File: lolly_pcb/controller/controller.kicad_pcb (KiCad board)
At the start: 2 copper layers, 93.8 x 60.6 mm, 81 parts, among them J1 Conn_01x02_Pin, SW1 SW_SPDT, U1 ESP32-S2-MINI-1

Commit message: use pin no. 5 for button
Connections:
- U1 pad VBUS: VBUS -> (no net)
- U4 pad 1: 11 -> 5
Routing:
- net VBUS: track 87.8 -> 11.1 mm, vias 2 -> 0
- net 11: track 96.3 -> 70.1 mm, vias 4 -> 3
- net 5: track 71.2 -> 93.4 mm, vias 3 -> 5
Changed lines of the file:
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@@
 			(layers "*.Cu" "*.Mask")
 			(remove_unused_layers no)
-			(net 9 "11")
+			(net 25 "5")
 			(pinfunction "In1")
 			(pintype "input")
@@
 			(layers "*.Cu" "*.Mask")
 			(remove_unused_layers no)
-			(net 30 "VBUS")
 		)
 	)
@@
 	)
 	(gr_text "Bat+\n"
-		(at 155.461 135.56 0)
+		(at 145.682 132.385 0)
 		(layer "B.SilkS")
 		(effects
@@
 	)
 	(gr_text "Bat -\n"
-		(at 161.938 127.813 0)
+		(at 153.048 132.385 0)
 		(layer "B.SilkS")
 		(effects
@@
 	)
 	(segment
-		(start 147.46 140.64)
-		(end 153.81 134.29)
-		(width 0.2)
-		(layer "F.Cu")
-		(net 9)
-	)
-	(segment
 		(start 117.742 123.114)
 		(end 116.98 122.352)
@@
 	)
 	(segment
-		(start 147.46 148.514)
-		(end 147.46 140.64)
-		(width 0.2)
-		(layer "F.Cu")
-		(net 9)
-	)
-	(segment
 		(start 145.682 122.86)
 		(end 145.428 123.114)
@@
 	)
 	(via
-		(at 153.81 134.29)
-		(size 0.6)
-		(drill 0.3)
-		(layers "F.Cu" "B.Cu")
-		(net 9)
-	)
-	(via
 		(at 145.682 122.86)
 		(size 0.6)
@@
 	)
 	(segment
-		(start 153.81 134.29)
-		(end 153.81 126.67)
-		(width 0.2)
-		(layer "B.Cu")
-		(net 9)
-	)
-	(segment
-		(start 156.604 125.4)
-		(end 155.08 125.4)
+		(start 148.222 125.4)
+		(end 156.604 125.4)
 		(width 0.2)
 		(layer "B.Cu")
@@
 	)
 	(segment
-		(start 153.81 126.67)
-		(end 155.08 125.4)
-		(width 0.2)
-		(layer "B.Cu")
-		(net 9)
-	)
-	(segment
-		(start 155.08 125.4)
-		(end 148.222 125.4)
-		(width 0.2)
-		(layer "B.Cu")
-		(net 9)
-	)
-	(segment
 		(start 148.222 125.4)
 		(end 145.682 122.86)
@@
 	)
 	(segment
+		(start 147.46 135.687)
+		(end 149.365 133.782)
+		(width 0.2)
+		(layer "F.Cu")
+		(net 25)
+	)
+	(segment
 		(start 124.6 120.066)
 		(end 124.6 107.62)
@@
 	)
 	(segment
+		(start 147.46 148.514)
+		(end 147.46 135.687)
+		(width 0.2)
+		(layer "F.Cu")
+		(net 25)
+	)
+	(segment
 		(start 146.698 127.686)
 		(end 143.396 124.384)
@@
 	)
 	(via
+		(at 150.762 127.686)
+		(size 0.6)
+		(drill 0.3)
+		(layers "F.Cu" "B.Cu")
+		(net 25)
+	)
+	(via
 		(at 161.176 127.686)
 		(size 0.6)
@@
 		(net 25)
 	)
+	(via
+		(at 149.365 133.782)
+		(size 0.6)
+		(drill 0.3)
+		(layers "F.Cu" "B.Cu")
+		(net 25)
+	)
 	(segment
 		(start 174.384 127.686)
@@
 	)
 	(segment
+		(start 150 128.448)
+		(end 150.762 127.686)
+		(width 0.2)
+		(layer "B.Cu")
+		(net 25)
+	)
+	(segment
 		(start 131.204 122.352)
 		(end 131.712 122.86)
@@
 	)
 	(segment
+		(start 149.365 133.782)
+		(end 150 133.147)
+		(width 0.2)
+		(layer "B.Cu")
+		(net 25)
+	)
+	(segment
+		(start 150 133.147)
+		(end 150 128.448)
+		(width 0.2)
+		(layer "B.Cu")
+		(net 25)
+	)
+	(segment
 		(start 143.269 124.384)
 		(end 143.396 124.384)
@@
 	)
 	(segment
-		(start 158.5 111.5)
-		(end 158.5 109.1)
-		(width 0.5)
-		(layer "F.Cu")
-		(net 30)
-	)
-	(via
-		(at 158.5 111.5)
-		(size 0.6)
-		(drill 0.3)
-		(layers "F.Cu" "B.Cu")
-		(net 30)
-	)
-	(via
-		(at 158.5 109.1)
-		(size 0.6)
-		(drill 0.3)
-		(layers "F.Cu" "B.Cu")
-		(net 30)
-	)
-	(segment
-		(start 161.6 140.6)
-		(end 161.6 139.032)
-		(width 0.5)
-		(layer "B.Cu")
-		(net 30)
-	)
-	(segment
 		(start 168.844179 146.986364)
 		(end 165.486364 146.986364)
@@
 	)
 	(segment
-		(start 162.49 109.1)
-		(end 165.24 106.35)
-		(width 0.5)
-		(layer "B.Cu")
-		(net 30)
-	)
-	(segment
-		(start 136.70583 101.973744)
-		(end 136.664953 101.932867)
-		(width 0.5)
-		(layer "B.Cu")
-		(net 30)
-	)
-	(segment
-		(start 158.5 135.932)
-		(end 158.5 111.5)
-		(width 0.5)
-		(layer "B.Cu")
-		(net 30)
-	)
-	(segment
-		(start 136.664953 101.932867)
-		(end 135.395 103.20282)
-		(width 0.5)
-		(layer "B.Cu")
-		(net 30)
-	)
-	(segment
-		(start 135.395 103.20282)
-		(end 135.395 105.08)
-		(width 0.5)
-		(layer "B.Cu")
-		(net 30)
-	)
-	(segment
-		(start 165.24 106.35)
-		(end 160.863744 101.973744)
-		(width 0.5)
-		(layer "B.Cu")
-		(net 30)
-	)
-	(segment
-		(start 158.5 109.1)
-		(end 162.49 109.1)
-		(width 0.5)
-		(layer "B.Cu")
-		(net 30)
-	)
-	(segment
 		(start 165.486364 146.986364)
 		(end 160 141.5)
 		(width 0.5)
 		(layer "B.Cu")
-		(net 30)
-	)
-	(segment
-		(start 160.863744 101.973744)
-		(end 136.70583 101.973744)
-		(width 0.5)
-		(layer "B.Cu")
-		(net 30)
-	)
-	(segment
-		(start 161.6 139.032)
-		(end 158.5 135.932)
-		(width 0.5)
-		(layer "B.Cu")
-		(net 30)
-	)
-	(segment
-		(start 160.7 141.5)
-		(end 161.6 140.6)
-		(width 0.5)
-		(layer "B.Cu")
-		(net 30)
-	)
-	(segment
-		(start 160 141.5)
-		(end 160.7 141.5)
-		(width 0.5)
-		(layer "B.Cu")

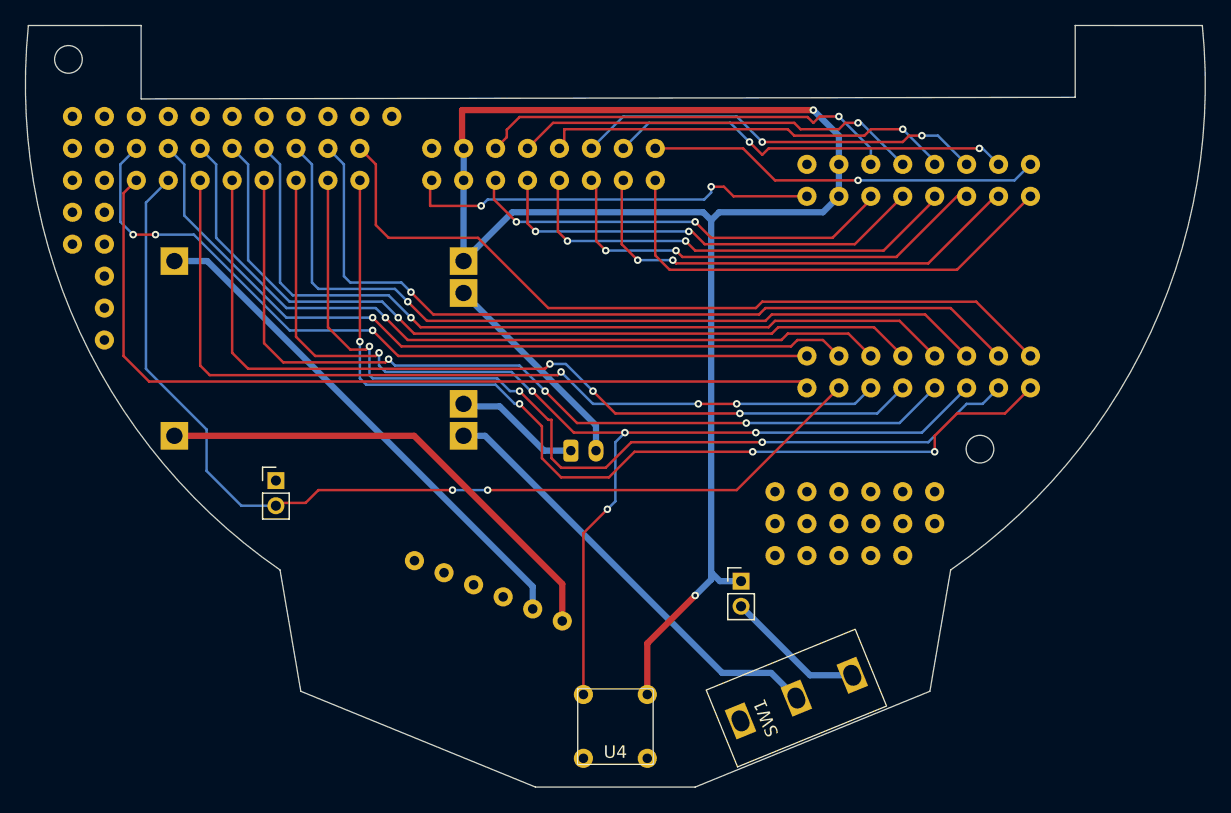
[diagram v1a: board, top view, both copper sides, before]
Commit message: fix controller hole positions and sizes
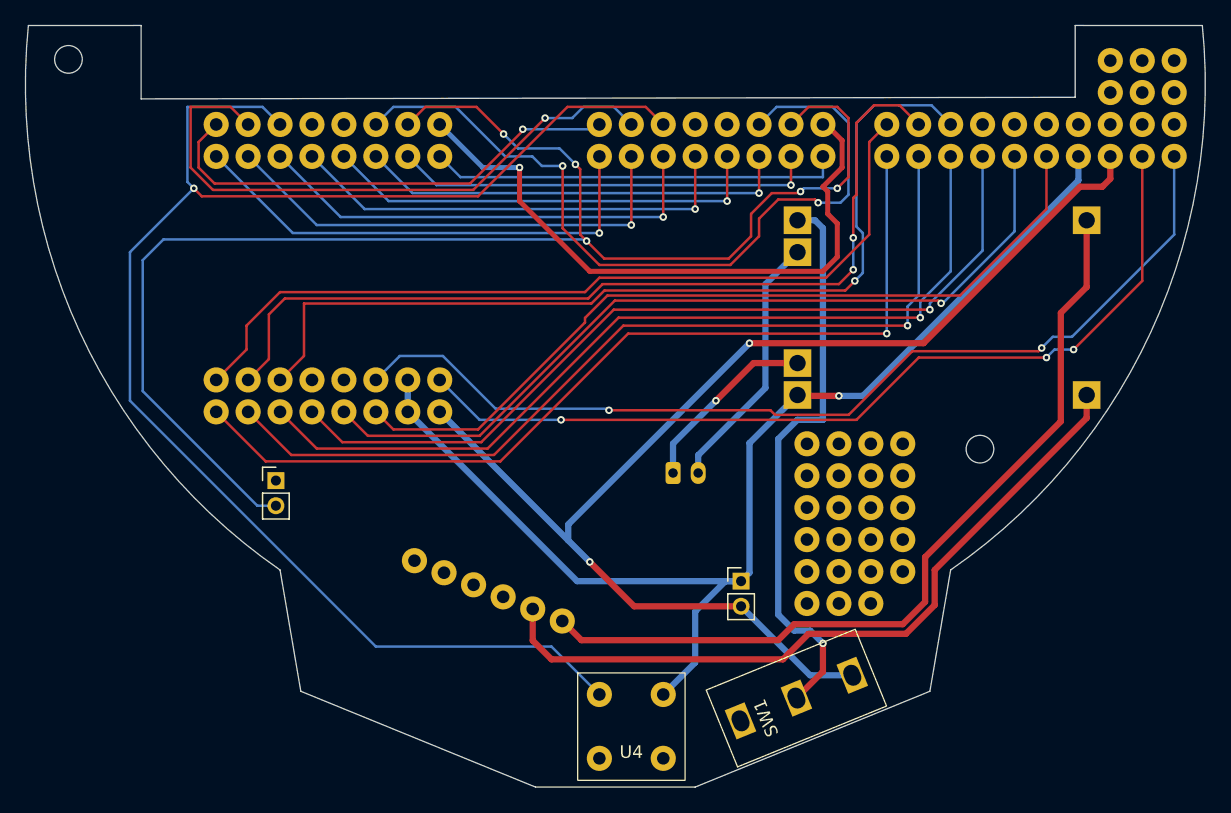
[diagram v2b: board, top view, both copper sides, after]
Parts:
- removed the ? at (170.3, 134.9)
- removed the ? at (106.8, 107.6)
- removed the ? at (175.4, 132.4)
- removed the ? at (162.7, 134.9)
- removed the ? at (175.4, 134.9)
- removed the ? at (106.8, 112.7)
- removed the ? at (167.8, 137.5)
- removed the ? at (165.2, 132.4)
- removed the ? at (127.1, 102.5)
- removed the ? at (111.9, 102.5)
- removed the ? at (109.4, 117.8)
- removed the ? at (109.4, 110.2)
- removed the ? at (162.7, 137.5)
- removed the ? at (165.2, 134.9)
- removed the ? at (109.4, 115.2)
- removed the ? at (119.5, 102.5)
- removed the ? at (109.4, 107.6)
- removed the ? at (129.7, 102.5)
- removed the ? at (165.2, 137.5)
- removed the ? at (109.4, 105.1)
- removed the ? at (124.6, 102.5)
- removed the ? at (167.8, 134.9)
- removed the ? at (172.9, 137.5)
- removed the ? at (109.4, 102.5)
- removed the ? at (106.8, 102.5)
- removed the ? at (172.9, 134.9)
- removed the ? at (172.9, 132.4)
- removed the ? at (106.8, 110.2)
- removed the ? at (122.1, 102.5)
- removed the ? at (109.4, 120.3)
- removed the ? at (162.7, 132.4)
- removed the ? at (106.8, 105.1)
- removed the ? at (132.2, 102.5)
- removed the ? at (109.4, 112.7)
- removed the ? at (122.1, 107.6)
- removed the ? at (119.5, 105.1)
- removed the ? at (111.9, 107.6)
- removed the ? at (143.0, 107.6)
- removed the ? at (143.0, 105.1)
- removed the ? at (111.9, 105.1)
- removed the ? at (135.4, 107.6)
- removed the ? at (129.7, 107.6)
- removed the ? at (135.4, 105.1)
- removed the ? at (124.6, 105.1)
- removed the ? at (167.8, 132.4)
- removed the ? at (129.7, 105.1)
- removed the ? at (148.1, 105.1)
- removed the ? at (145.6, 107.6)
- removed the ? at (114.4, 105.1)
- removed the ? at (140.5, 107.6)
- removed the ? at (148.1, 107.6)
- removed the ? at (127.1, 105.1)
- removed the ? at (150.6, 107.6)
- removed the ? at (122.1, 105.1)
- removed the ? at (114.4, 107.6)
- removed the ? at (117.0, 102.5)
- removed the ? at (137.9, 107.6)
- removed the ? at (117.0, 105.1)
- removed the ? at (145.6, 105.1)
- removed the ? at (137.9, 105.1)
- removed the ? at (150.6, 105.1)
- removed the ? at (153.2, 107.6)
- removed the ? at (117.0, 107.6)
- removed the ? at (127.1, 107.6)
- removed the ? at (140.5, 105.1)
- removed the ? at (153.2, 105.1)
- removed the ? at (170.3, 137.5)
- removed the ? at (124.6, 107.6)
- removed the ? at (119.5, 107.6)
- removed the ? at (114.4, 102.5)
- removed the ? at (170.3, 132.4)
- added ?: , , F.Cu at (194.4, 105.7)
- added ?: , , F.Cu at (153.8, 103.2)
- added ?: , , F.Cu at (158.9, 105.7)
- added ?: , , F.Cu at (170.3, 136.2)
- added ?: , , F.Cu at (158.9, 103.2)
- added ?: , , F.Cu at (186.8, 103.2)
- added ?: , , F.Cu at (172.9, 128.6)
- added ?: , , F.Cu at (184.3, 105.7)
- added ?: , , F.Cu at (170.3, 138.7)
- added ?: , , F.Cu at (167.8, 138.7)
- added ?: , , F.Cu at (165.2, 141.3)
- added ?: , , F.Cu at (164.0, 105.7)
- added ?: , , F.Cu at (166.5, 105.7)
- added ?: , , F.Cu at (189.4, 100.6)
- added ?: , , F.Cu at (170.3, 141.3)
- added ?: , , F.Cu at (194.4, 100.6)
- added ?: , , F.Cu at (179.2, 103.2)
- added ?: , , F.Cu at (156.3, 105.7)
- added ?: , , F.Cu at (189.4, 98.1)
- added ?: , , F.Cu at (170.3, 131.1)
- added ?: , , F.Cu at (151.3, 105.7)
- added ?: , , F.Cu at (184.3, 103.2)
- added ?: , , F.Cu at (191.9, 103.2)
- added ?: , , F.Cu at (165.2, 131.1)
- added ?: , , F.Cu at (167.8, 133.7)
- added ?: , , F.Cu at (172.9, 133.7)
- added ?: , , F.Cu at (165.2, 138.7)
- added ?: , , F.Cu at (170.3, 133.7)
- added ?: , , F.Cu at (153.8, 105.7)
- added ?: , , F.Cu at (164.0, 103.2)
- added ?: , , F.Cu at (148.7, 105.7)
- added ?: , , F.Cu at (167.8, 128.6)
- added ?: , , F.Cu at (167.8, 136.2)
- added ?: , , F.Cu at (191.9, 105.7)
- added ?: , , F.Cu at (170.3, 128.6)
- added ?: , , F.Cu at (148.7, 103.2)
- added ?: , , F.Cu at (156.3, 103.2)
- added ?: , , F.Cu at (172.9, 136.2)
- added ?: , , F.Cu at (179.2, 105.7)
- added ?: , , F.Cu at (166.5, 103.2)
- added ?: , , F.Cu at (181.8, 103.2)
- added ?: , , F.Cu at (194.4, 98.1)
- added ?: , , F.Cu at (151.3, 103.2)
- added ?: , , F.Cu at (161.4, 105.7)
- added ?: , , F.Cu at (165.2, 133.7)
- added ?: , , F.Cu at (181.8, 105.7)
- added ?: , , F.Cu at (194.4, 103.2)
- added ?: , , F.Cu at (189.4, 105.7)
- added ?: , , F.Cu at (167.8, 141.3)
- added ?: , , F.Cu at (165.2, 128.6)
- added ?: , , F.Cu at (191.9, 100.6)
- added ?: , , F.Cu at (186.8, 105.7)
- added ?: , , F.Cu at (167.8, 131.1)
- added ?: , , F.Cu at (189.4, 103.2)
- added ?: , , F.Cu at (165.2, 136.2)
- added ?: , , F.Cu at (172.9, 131.1)
- added ?: , , B.Cu at (171.6, 103.2)
- added ?: , , B.Cu at (174.1, 105.7)
- added ?: , , B.Cu at (176.7, 105.7)
- added ?: , , B.Cu at (176.7, 103.2)
- added ?: , , B.Cu at (171.6, 105.7)
- added ?: , , B.Cu at (174.1, 103.2)
- added ?: , , F.Cu at (172.9, 138.7)
- added ?: , , F.Cu at (191.9, 98.1)
- added ?: , , F.Cu at (161.4, 103.2)
- moved U2 74.6 mm to (187.5, 110.8), turned to 180 degrees
- moved U1 54.6 mm to (123.3, 114.6), turned to -90 degrees
- moved J1 8.32 mm to (154.6, 130.9)
- moved U4 1.27 mm to (151.3, 153.6)
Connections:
- J1 pad 1: Bat+ -> Bat-
- J1 pad 2: Bat- -> Bat+
- U1 pad VBUS: (no net) -> VBUS
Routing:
- net VBUS: track 11.1 -> 99.0 mm, vias 0 -> 2
- net 7: track 70.3 -> 0.00 mm, vias 3 -> 0
- net 9: track 70.2 -> 0.00 mm, vias 3 -> 0
- net 17: track 33.9 -> 78.4 mm
- net 39: track 31.4 -> 73.3 mm
- net EN: track 77.5 -> 37.9 mm, vias 4 -> 1
- net 37: track 32.5 -> 72.0 mm, vias 2 -> 1
- net 15: track 33.1 -> 71.7 mm, vias 2 -> 3
- net 12: track 80.8 -> 118.4 mm, vias 2 -> 5
- net 35: track 32.9 -> 70.3 mm, vias 2 -> 1
- net 36: track 36.4 -> 73.2 mm, vias 2 -> 1
- net 33: track 32.1 -> 68.4 mm
- net 34: track 36.2 -> 0.00 mm, vias 2 -> 0
- net 21: track 35.5 -> 0.00 mm, vias 2 -> 0
- net 18: track 32.5 -> 67.0 mm
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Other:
- board text added: "Mini Lolly Controller V2"
- board text removed: "21"
- board text removed: "34"
- board text removed: "7"
- board text removed: "9"
- board text removed: "Mini Lolly Controller V1"
